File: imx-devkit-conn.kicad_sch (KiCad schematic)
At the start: 16 parts, among them J8 PinHeader_2x10_P1.27mm_SMD_Sh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, U37 TCA9548ARGER

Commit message: [#83609] Reannotate board
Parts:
- renumbered C156 to C175, J8 to J14, R267 to R327, R268 to R328, R265 to R329, R266 to R330, R269 to R331, R270 to R332, R273 to R333, R271 to R334, R274 to R335, R272 to R336, R275 to R337, TP68 to TP28, TP69 to TP29, U37 to U41

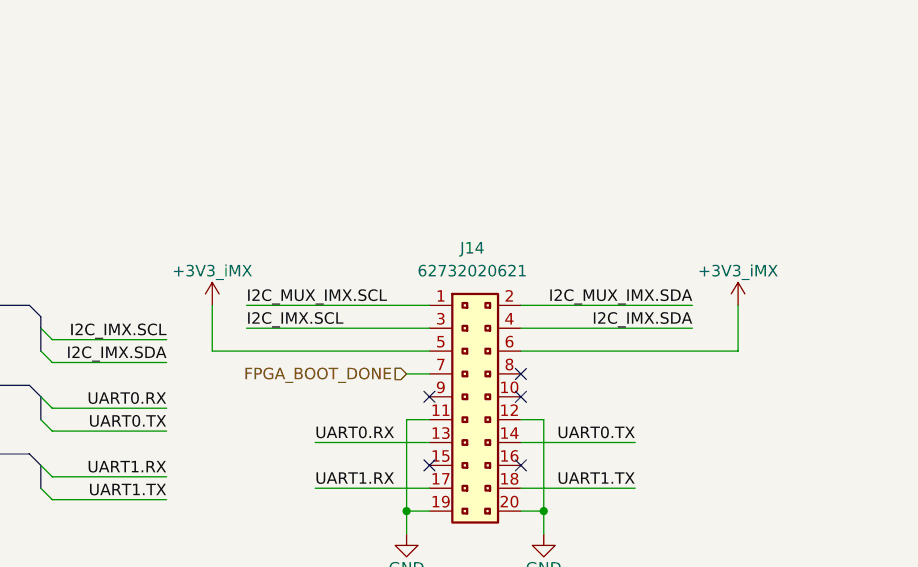
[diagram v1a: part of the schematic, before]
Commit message: [#83736] Update devkit connectors pinout
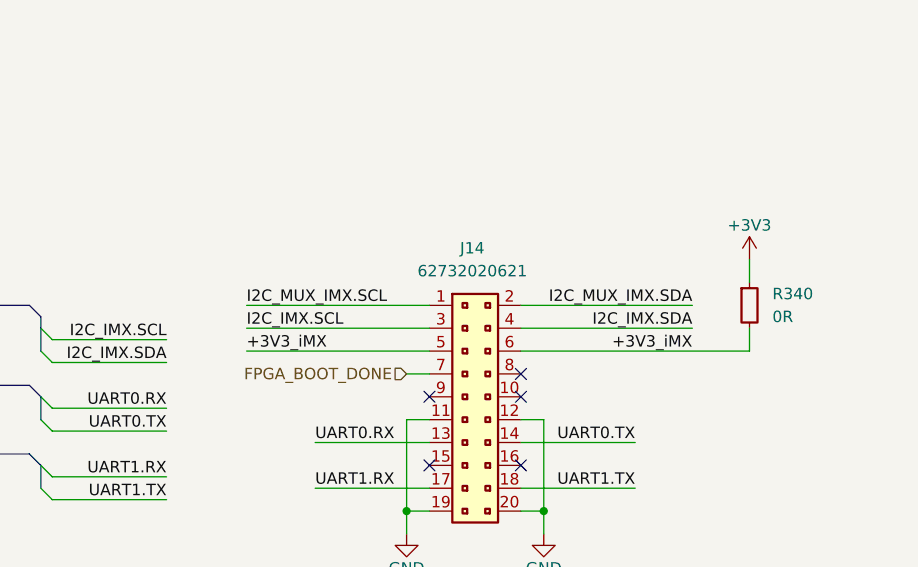
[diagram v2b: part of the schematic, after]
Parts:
- added R340: R_0R_0402, antmicro-footprints:R_0402_1005Metric, symbol antmicroResistors0402:R_0R_0402
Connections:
- net +3V3: now also R340.1
- net +3V3_iMX: now also R340.2

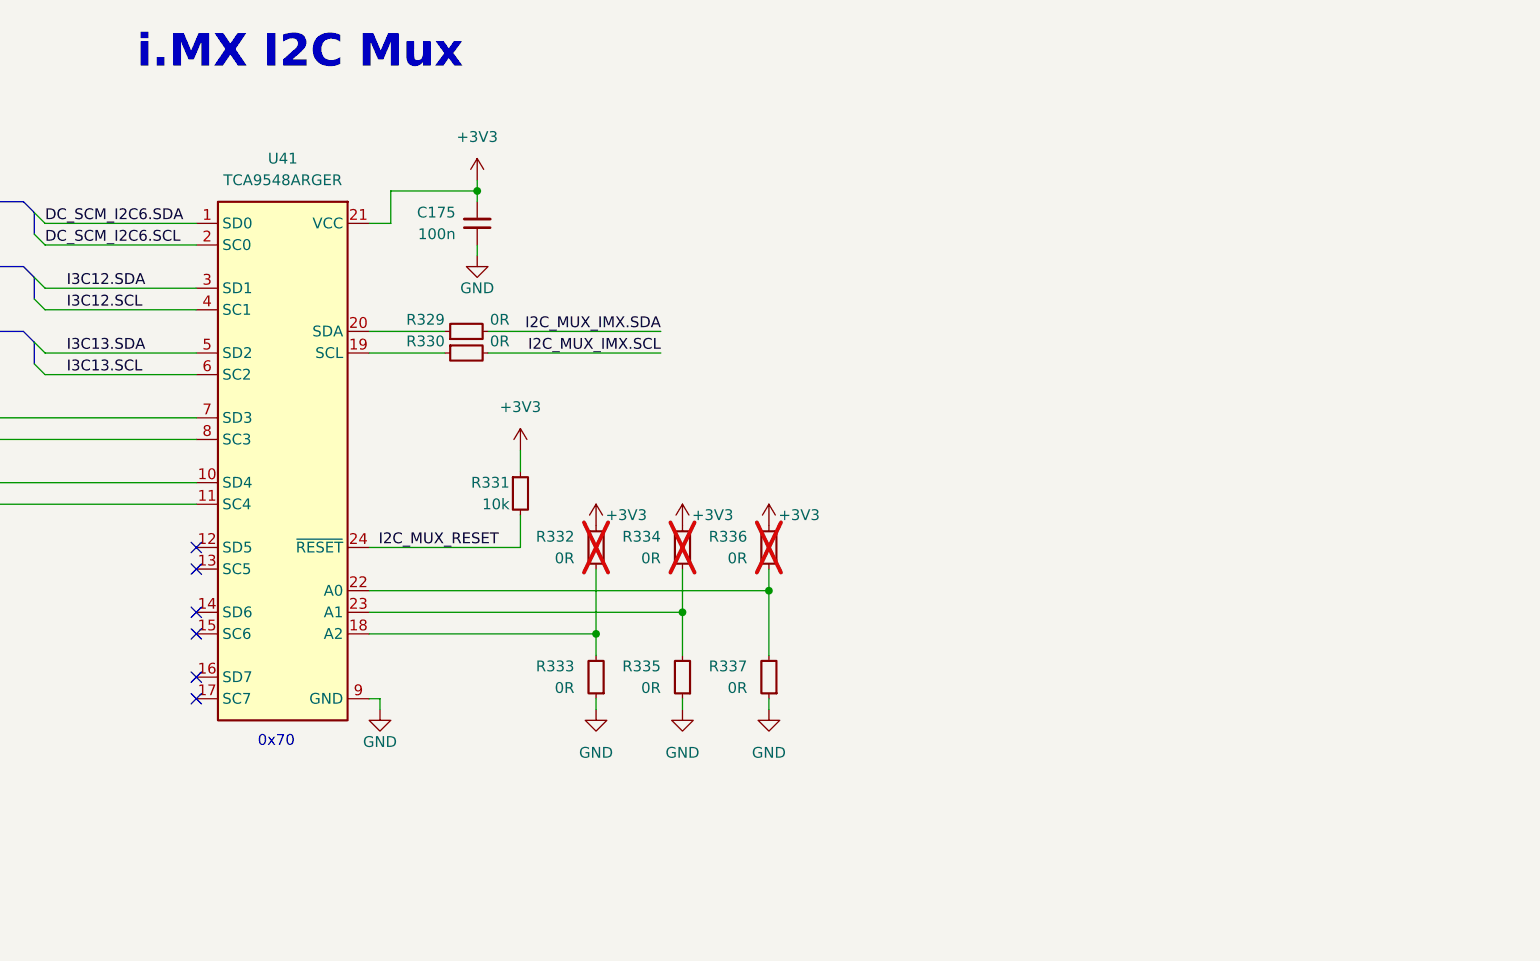
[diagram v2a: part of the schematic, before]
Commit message: [#83767] Add more I2C connections
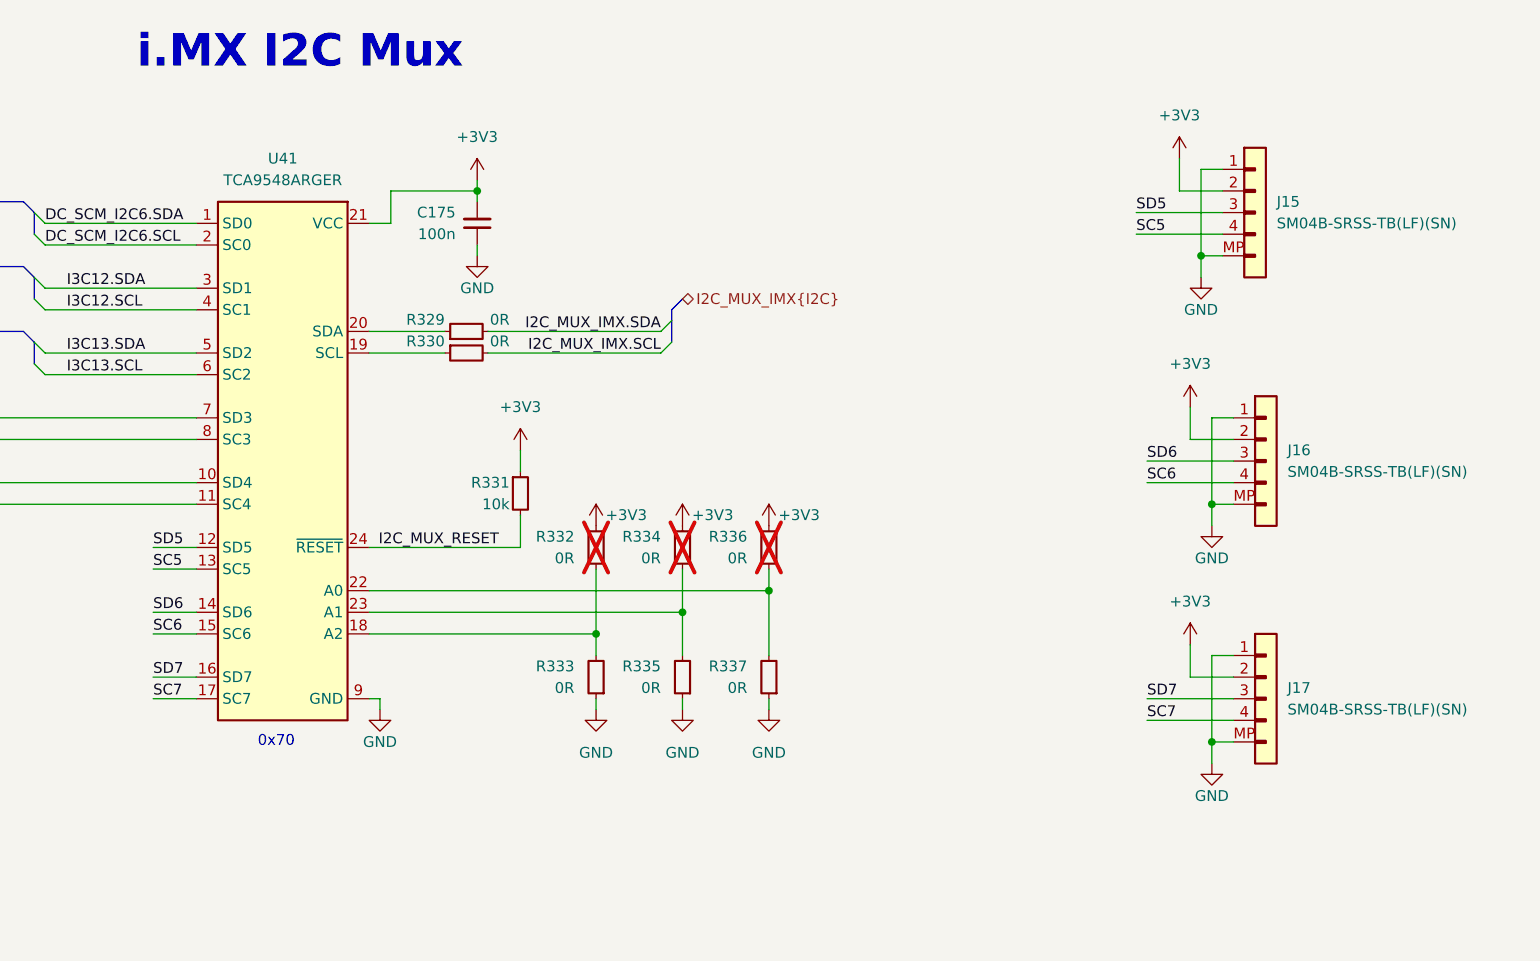
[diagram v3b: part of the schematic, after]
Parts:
- added J15, J16, J17: JST_SH_1x4_SM04B-SRSS-TB-LF-SN, antmicro-footprints:Conn_JST_SH_1x4_SM04B-SRSS-TB-LF-SN, symbol antmicroWire2BoardConnectors:JST_SH_1x4_SM04B-SRSS-TB-LF-SN
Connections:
- net +3V3: now also J15.2, J16.2, J17.2
- net GND: now also J15.1, J15.MP, J16.1, J16.MP, J17.1, J17.MP
- net SD5: now reaches U41.12 (SD5)
- net SD5: now also J15.3
- net SC5: now reaches U41.13 (SC5)
- net SC5: now also J15.4
- net SD6: now reaches U41.14 (SD6)
- net SD6: now also J16.3
- net SC6: now reaches U41.15 (SC6)
- net SC6: now also J16.4
- net SD7: now reaches U41.16 (SD7)
- net SD7: now also J17.3
- net SC7: now reaches U41.17 (SC7)
- net SC7: now also J17.4
- no-connect marks 11 -> 5

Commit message: [#83767] Route LTPI
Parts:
- removed J15, J16, J17: JST_SH_1x4_SM04B-SRSS-TB-LF-SN, antmicro-footprints:Conn_JST_SH_1x4_SM04B-SRSS-TB-LF-SN, symbol antmicroWire2BoardConnectors:JST_SH_1x4_SM04B-SRSS-TB-LF-SN
- added J15, J16, J3: JST_SH_1x4_BM04B-SRSS-TB-LF-SN, antmicro-footprints:Conn_JST_SH_1x4_BM04B-SRSS-TB-LF-SN, symbol antmicroWire2BoardConnectors:JST_SH_1x4_BM04B-SRSS-TB-LF-SN
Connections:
- net +3V3: now also J15.2, J16.2, J3.2
- net GND: now also J15.1, J15.MP, J16.1, J16.MP, J3.1, J3.MP
- net SC5: now also J3.4
- net SC6: now also J15.4
- net SC7: now also J16.4
- net SD5: now also J3.3
- net SD6: now also J15.3
- net SD7: now also J16.3
